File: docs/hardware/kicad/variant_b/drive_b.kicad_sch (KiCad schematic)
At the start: 11 parts, among them U40 74LVC08, U41 MDD20A front, U42 MDD20A rear, U43 CS FL, U44 CS FR, U45 CS RL, U46 CS RR

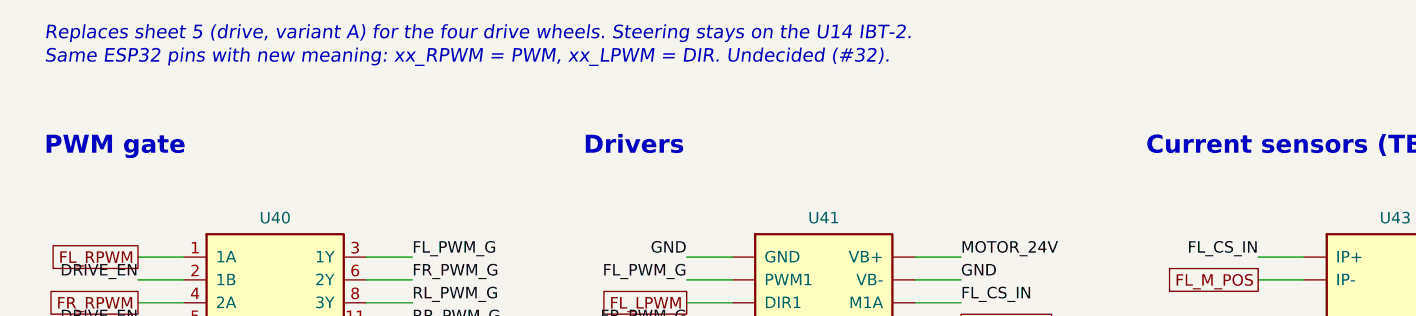
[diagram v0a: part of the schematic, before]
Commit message: Schematic: add a system wiring overview page (every assembly joined on one A2 sheet)
Page 2 is a drawing-only overview generated by gen/overview.py; the net
sheets move to pages 3-9. ERC and the netlist check are unchanged.

Co-Authored-By: Claude Opus 5.5 (1M context) <noreply@anthropic.com>
Claude-Session: https://claude.ai/code/session_01BSRw381bu7GTvawcDjL4S1
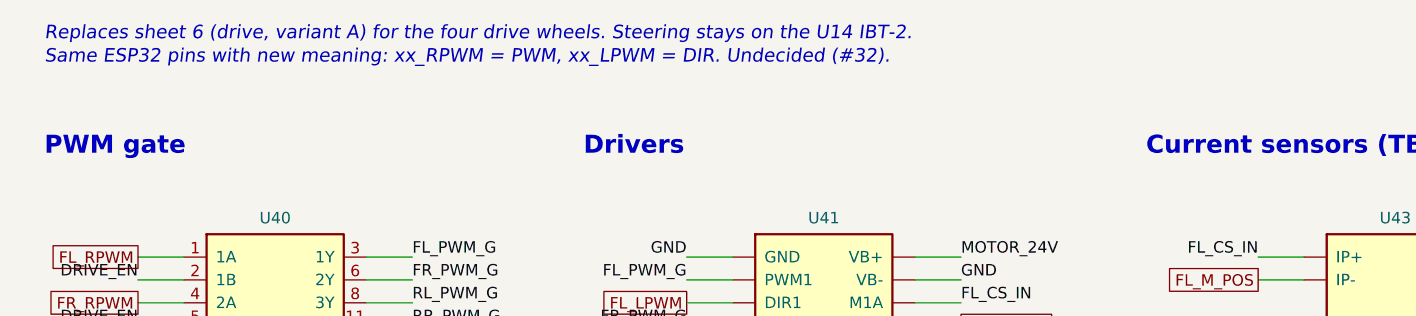
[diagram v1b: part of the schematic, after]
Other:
- note added: "Replaces sheet 6 (drive, variant A) for the four drive wheels. Steering stays on the U14 IBT-2."
- note removed: "Replaces sheet 5 (drive, variant A) for the four drive wheels. Steering stays on the U14 IBT-2."
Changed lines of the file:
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@@
 (wire (pts (xy 200.66 81.28) (xy 200.66 86.36)) (stroke (width 0) (type default)))
 (label "3V3_SENSE" (at 200.66 86.36 270) (effects (font (size 1.27 1.27)) (justify right bottom)))
-(text "Replaces sheet 5 (drive, variant A) for the four drive wheels. Steering stays on the U14 IBT-2." (exclude_from_sim no) (at 15 15 0) (effects (font (size 1.5 1.5) (italic yes)) (justify left top)))
+(text "Replaces sheet 6 (drive, variant A) for the four drive wheels. Steering stays on the U14 IBT-2." (exclude_from_sim no) (at 15 15 0) (effects (font (size 1.5 1.5) (italic yes)) (justify left top)))
 (text "Same ESP32 pins with new meaning: xx_RPWM = PWM, xx_LPWM = DIR. Undecided (#32)." (exclude_from_sim no) (at 15 17.6 0) (effects (font (size 1.5 1.5) (italic yes)) (justify left top)))
 (embedded_fonts no)
